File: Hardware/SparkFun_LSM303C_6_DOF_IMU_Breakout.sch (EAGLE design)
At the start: 27 parts, among them Q1 2.5A/30V, U1 LSM303C, U2 LM3880

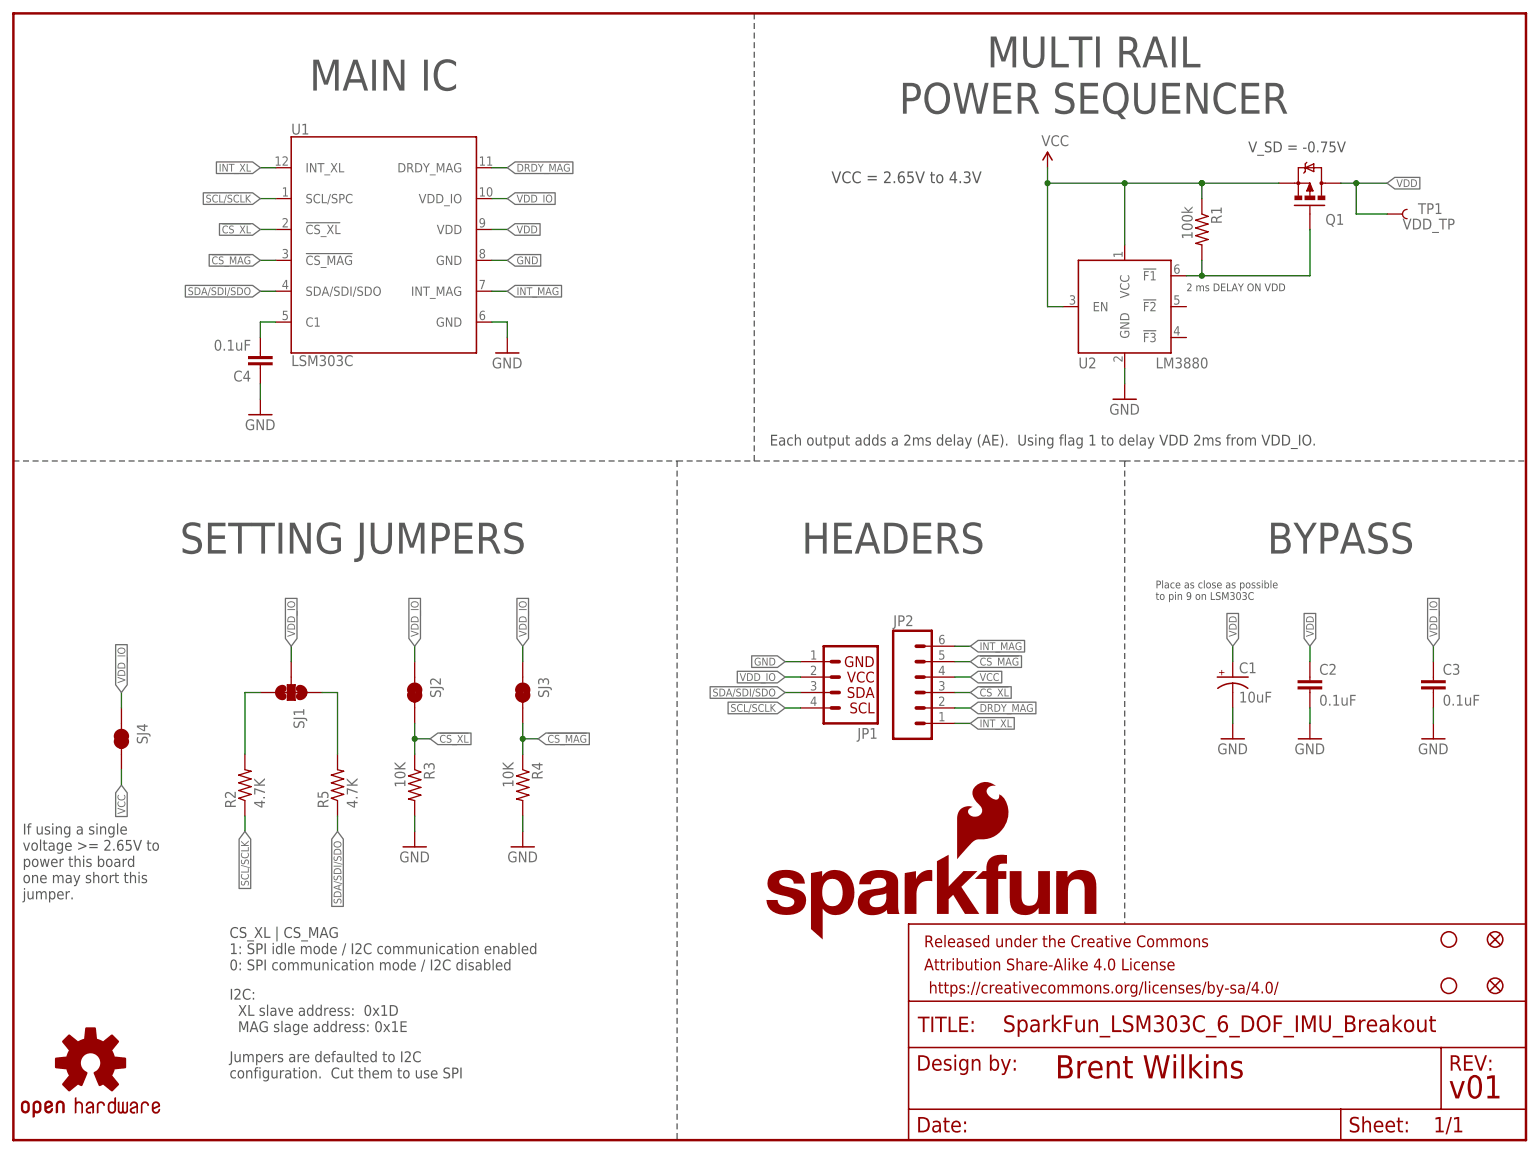
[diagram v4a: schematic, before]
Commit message: Fixed logic inversion bug and simplified board by removing jumpers
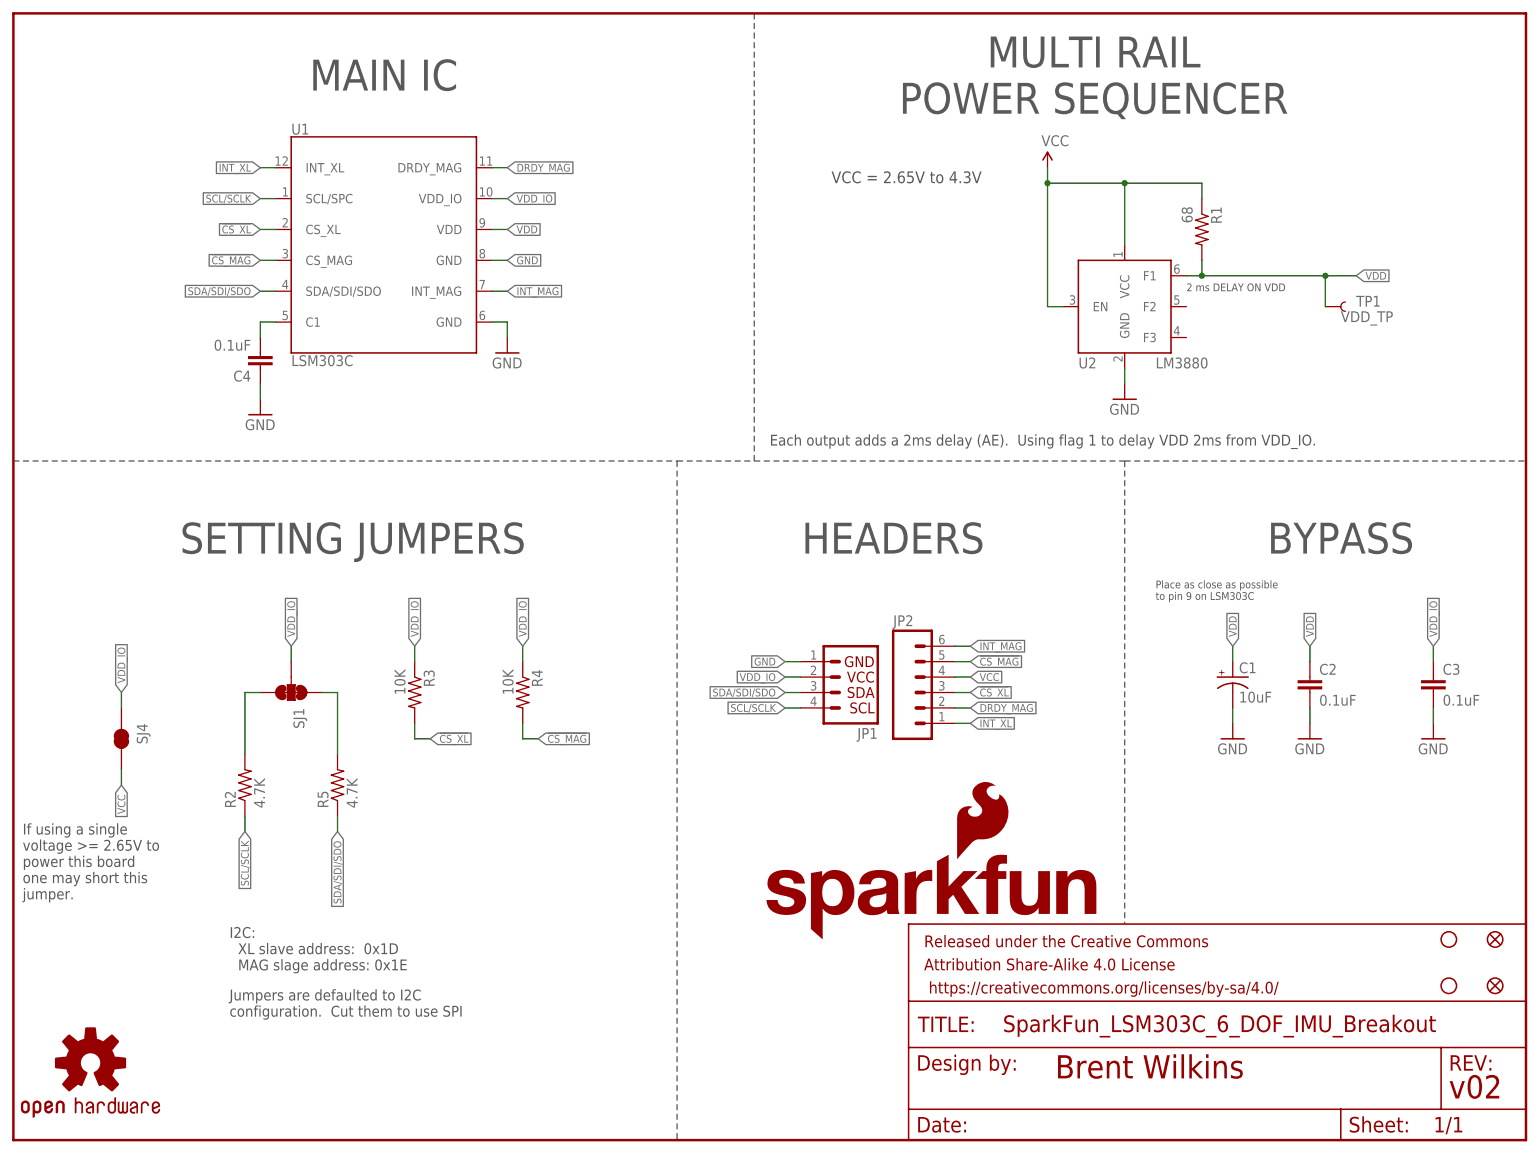
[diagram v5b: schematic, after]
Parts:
- removed Q1: 2.5A/30V, SparkFun-DiscreteSemi:MOSFET-PCHANNELDMG2307L
- removed SJ2, SJ3: JUMPER-PAD-2-NC_BY_TRACE, SparkFun-Passives:JUMPER-PAD-2-NC_BY_TRACE
- FRAME1: value (none) -> FRAME-LETTER; DESIGNER Brent Wilkins -> (none)
- R1: value 100k -> 68
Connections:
- removed net N$3: Q1.G, R1.2, U2.!F1
- net !CS_MAG: now also R4.2, U1.CS_MAG; no longer R4.1, SJ3.2, U1.!CS_MAG
- net !CS_XL: now also R3.2, U1.CS_XL; no longer R3.1, SJ2.2, U1.!CS_XL
- net GND: no longer R3.2, R4.2
- net VCC: no longer Q1.S
- net VDD: now also R1.2, U2.F1; no longer Q1.D
- net VDD_IO: now also R3.1, R4.1; no longer SJ2.1, SJ3.1
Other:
- note removed: "CS_XL | CS_MAG 1: SPI idle mode / I2C communication enabled 0: SPI communication mode / I2C disabled"
- note removed: "V_SD = -0.75V"
- moved on the sheet: R3, R4, TP1

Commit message: Updated SKU of 68Ω resistor
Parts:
- R1: PROD_ID RES-07828 -> RES-07860
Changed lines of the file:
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@@
 <?xml version="1.0" encoding="utf-8"?>
 <!DOCTYPE eagle SYSTEM "eagle.dtd">
-<eagle version="7.2.0">
+<eagle version="7.3.0">
 <drawing>
 <settings>
@@
 <part name="GND13" library="SparkFun-Aesthetics" deviceset="GND" device=""/>
 <part name="R1" library="SparkFun-Passives" deviceset="RESISTOR" device="0603-RES" value="68">
-<attribute name="PROD_ID" value="RES-07828"/>
+<attribute name="PROD_ID" value="RES-07860"/>
 </part>
 <part name="U2" library="SparkFun-DigitalIC" deviceset="LM3880/-QI" device="" value="LM3880">

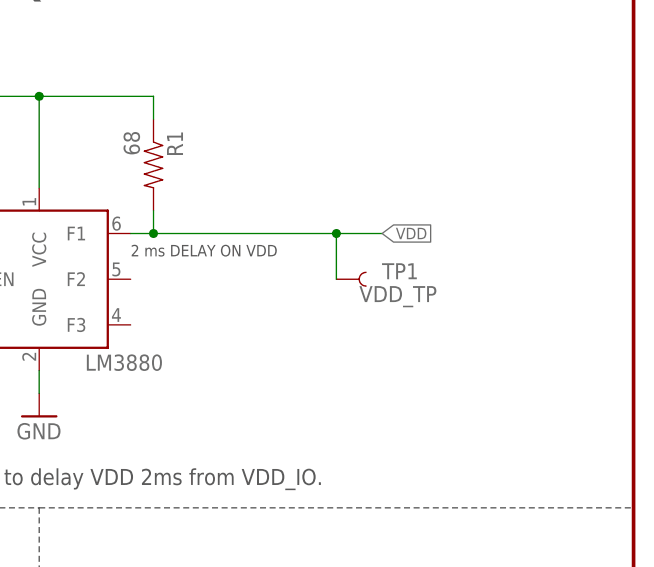
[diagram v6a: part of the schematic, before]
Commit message: Resolved QC issues
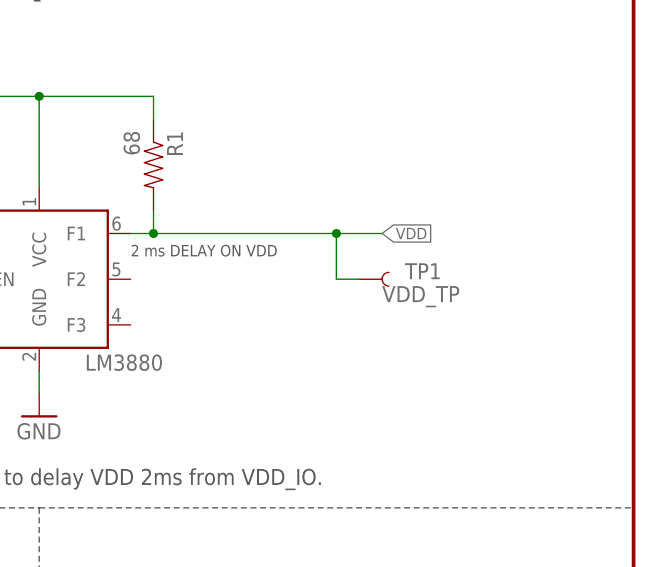
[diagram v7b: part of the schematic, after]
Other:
- moved on the sheet: TP1
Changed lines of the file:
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@@
 <?xml version="1.0" encoding="utf-8"?>
 <!DOCTYPE eagle SYSTEM "eagle.dtd">
-<eagle version="7.3.0">
+<eagle version="7.2.0">
 <drawing>
 <settings>
@@
 <attribute name="NAME" x="20.32" y="68.58" size="1.778" layer="95" rot="R270"/>
 </instance>
-<instance part="TP1" gate="G$1" x="215.9" y="137.16" smashed="yes">
-<attribute name="NAME" x="220.98" y="137.16" size="1.778" layer="95"/>
-<attribute name="VALUE" x="218.44" y="134.62" size="1.778" layer="96"/>
+<instance part="TP1" gate="G$1" x="218.44" y="137.16" smashed="yes">
+<attribute name="NAME" x="223.52" y="137.16" size="1.778" layer="95"/>
+<attribute name="VALUE" x="220.98" y="134.62" size="1.778" layer="96"/>
 </instance>
 <instance part="STANDOFF1" gate="G$1" x="236.22" y="25.4"/>
@@
 <label x="220.98" y="142.24" size="1.27" layer="95" xref="yes"/>
 <pinref part="TP1" gate="G$1" pin="1"/>
+<wire x1="218.44" y1="137.16" x2="215.9" y2="137.16" width="0.1524" layer="91"/>
 <wire x1="215.9" y1="137.16" x2="215.9" y2="142.24" width="0.1524" layer="91"/>
 <pinref part="R1" gate="G$1" pin="2"/>
